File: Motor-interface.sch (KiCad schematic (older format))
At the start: 5 parts, among them K1 RELAY_2RT, U1 MCP42010, U2 Teensy_3.2

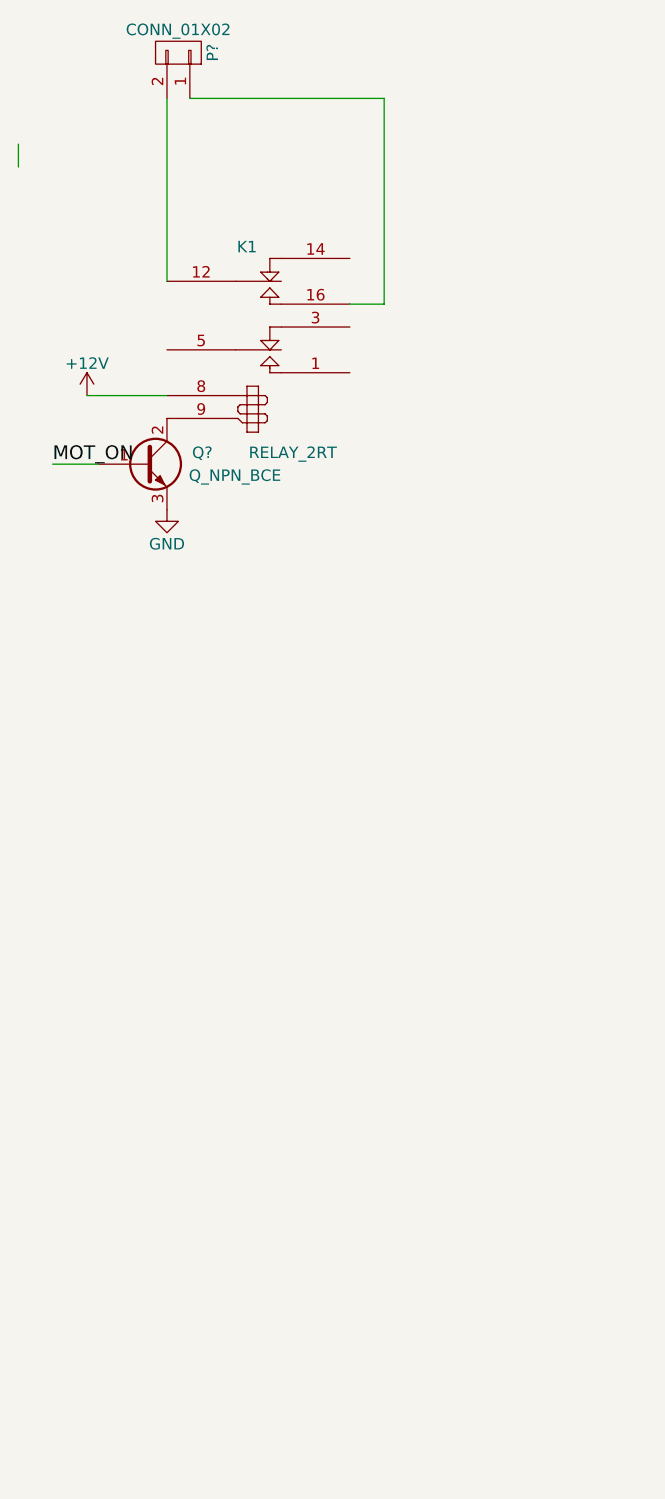
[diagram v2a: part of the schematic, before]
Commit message: Added TE 23pins and netlist
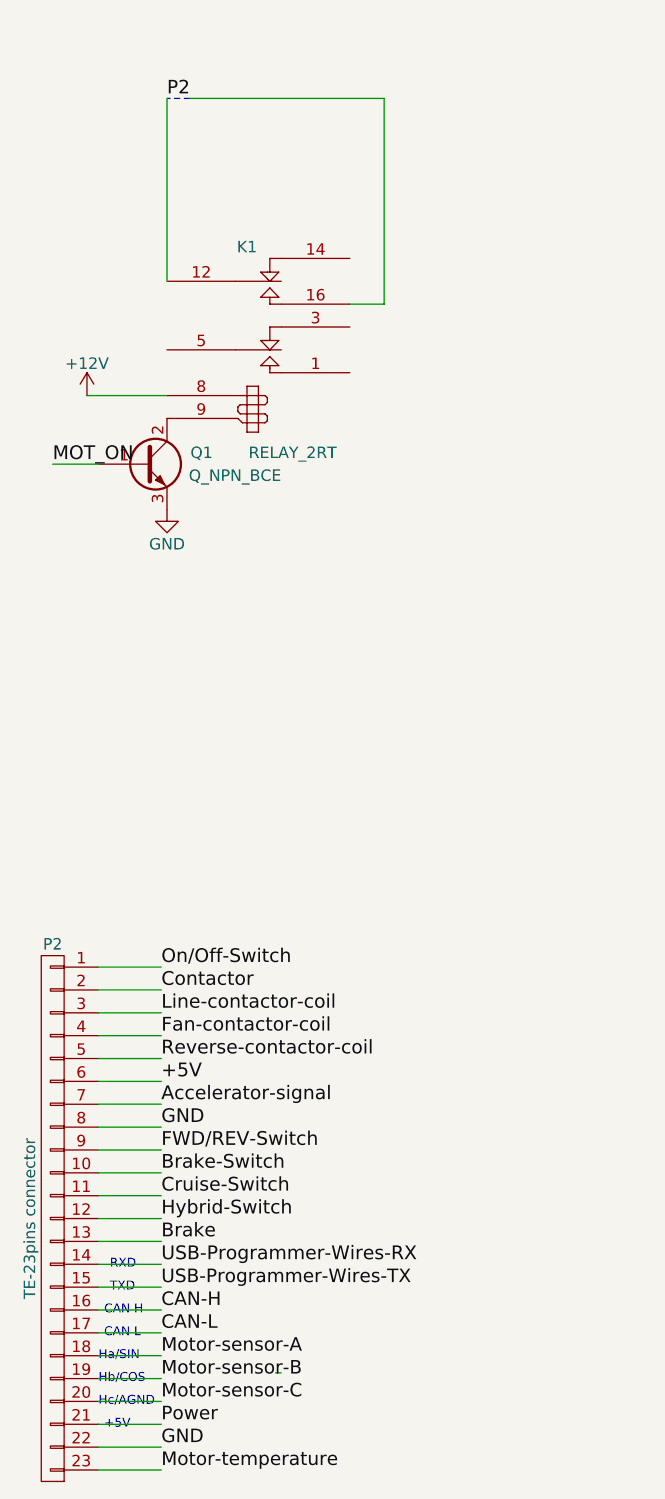
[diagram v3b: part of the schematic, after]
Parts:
- removed P?: CONN_01X02, symbol CONN_01X02
- added P2: TE-23pins connector, electric_car_lib:TE_23_pins_776087-1_connector, symbol CONN_01X23
- K1: footprint (none) -> Relays_ThroughHole:Relay_SANYOU_SRD_Series_Form_C
- Q1: renamed from Q?; footprint (none) -> TO_SOT_Packages_SMD:SOT-23
- U1: footprint (none) -> Housings_SOIC:SOIC-14_3.9x8.7mm_Pitch1.27mm
- U2: footprint (none) -> Housings_SSOP:TSSOP-32_6.1x11mm_Pitch0.65mm
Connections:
- net labels added: +5V, Accelerator-signal, Brake-Switch, CAN-H, CAN-L, Contactor, Cruise-Switch, FWD/REV-Switch, Fan-contactor-coil, Hybrid-Switch, Line-contactor-coil, Motor-sensor-A, Motor-sensor-B, Motor-sensor-C, Motor-temperature, On/Off-Switch, P2, Power, Reverse-contactor-coil, USB-Programmer-Wires-RX, USB-Programmer-Wires-TX
- wire segments 22 -> 45
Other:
- note added: "+5V"
- note added: "CAN H"
- note added: "CAN L"
- note added: "Ha/SIN"
- note added: "Hb/COS"
- note added: "Hc/AGND"
- note added: "RXD"
- note added: "TXD"
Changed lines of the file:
@@
 LIBS:contrib
 LIBS:valves
-LIBS:electric_car
 LIBS:Motor-interface-cache
 EELAYER 25 0
@@
 F 0 "U2" H 7050 2700 39  0000 C CNN
 F 1 "Teensy_3.2" H 7050 3400 39  0000 C CNN
-F 2 "" H 6750 2400 39  0000 C CNN
+F 2 "Housings_SSOP:TSSOP-32_6.1x11mm_Pitch0.65mm" H 6750 2400 39  0001 C CNN
 F 3 "" H 6750 2400 39  0000 C CNN
 	1    7050 2850
@@
 F 0 "U1" H 4850 2900 50  0000 L CNN
 F 1 "MCP42010" H 5250 2900 50  0000 L CNN
-F 2 "" H 5150 2550 50  0000 C CNN
+F 2 "Housings_SOIC:SOIC-14_3.9x8.7mm_Pitch1.27mm" H 5150 2550 50  0001 C CNN
 F 3 "" H 5150 2550 50  0000 C CNN
 	1    5150 2450
@@
 F 0 "K1" H 1850 2600 50  0000 C CNN
 F 1 "RELAY_2RT" H 2050 1700 50  0000 C CNN
-F 2 "" H 1900 2200 50  0000 C CNN
+F 2 "Relays_ThroughHole:Relay_SANYOU_SRD_Series_Form_C" H 1900 2200 50  0001 C CNN
 F 3 "" H 1900 2200 50  0000 C CNN
 	1    1900 2200
@@
 $EndComp
 $Comp
-L Q_NPN_BCE Q?
+L Q_NPN_BCE Q1
 U 1 1 57FCBE60
 P 1400 2750
-F 0 "Q?" H 1700 2800 50  0000 R CNN
+F 0 "Q1" H 1700 2800 50  0000 R CNN
 F 1 "Q_NPN_BCE" H 2000 2700 50  0000 R CNN
-F 2 "" H 1600 2850 50  0000 C CNN
+F 2 "TO_SOT_Packages_SMD:SOT-23" H 1600 2850 50  0001 C CNN
 F 3 "" H 1400 2750 50  0000 C CNN
 	1    1400 2750
@@
 	1150 2450 1500 2450
 $Comp
-L +12V #PWR?
+L +12V #PWR01
 U 1 1 57FCC08A
 P 1150 2450
-F 0 "#PWR?" H 1150 2300 50  0001 C CNN
+F 0 "#PWR01" H 1150 2300 50  0001 C CNN
 F 1 "+12V" H 1150 2590 50  0000 C CNN
 F 2 "" H 1150 2450 50  0000 C CNN
@@
 $EndComp
 $Comp
-L GND #PWR?
+L GND #PWR02
 U 1 1 57FCC1C9
 P 1500 2950
-F 0 "#PWR?" H 1500 2700 50  0001 C CNN
+F 0 "#PWR02" H 1500 2700 50  0001 C CNN
 F 1 "GND" H 1500 2800 50  0000 C CNN
 F 2 "" H 1500 2950 50  0000 C CNN
@@
 	6000 3250 6350 3250
 $Comp
-L +3.3V #PWR?
+L +3.3V #PWR03
 U 1 1 58059323
 P 3850 2150
-F 0 "#PWR?" H 3850 2000 50  0001 C CNN
+F 0 "#PWR03" H 3850 2000 50  0001 C CNN
 F 1 "+3.3V" H 3850 2290 50  0000 C CNN
 F 2 "" H 3850 2150 50  0000 C CNN
@@
 $EndComp
 $Comp
-L +3.3V #PWR?
+L +3.3V #PWR04
 U 1 1 5805934B
 P 3850 2550
-F 0 "#PWR?" H 3850 2400 50  0001 C CNN
+F 0 "#PWR04" H 3850 2400 50  0001 C CNN
 F 1 "+3.3V" H 3850 2690 50  0000 C CNN
 F 2 "" H 3850 2550 50  0000 C CNN
@@
 Wire Wire Line
 	3850 2550 4650 2550
-$Comp
-L CONN_01X02 P?
-U 1 1 5805A054
-P 1550 950
-F 0 "P?" H 1550 1100 50  0000 C CNN
-F 1 "CONN_01X02" V 1650 950 50  0000 C CNN
-F 2 "" H 1550 950 50  0000 C CNN
-F 3 "" H 1550 950 50  0000 C CNN
-	1    1550 950
-	0    1    -1   0
-$EndComp
-Wire Wire Line
-	850  1450 850  1350
 Wire Wire Line
 	1500 1150 1500 1950
@@
 	2450 2050 2300 2050
 $Comp
-L GND #PWR?
+L GND #PWR05
 U 1 1 5805B577
 P 4650 2350
-F 0 "#PWR?" H 4650 2100 50  0001 C CNN
+F 0 "#PWR05" H 4650 2100 50  0001 C CNN
 F 1 "GND" H 4650 2200 50  0000 C CNN
 F 2 "" H 4650 2350 50  0000 C CNN
@@
 $EndComp
 $Comp
-L GND #PWR?
+L GND #PWR06
 U 1 1 5805B5A1
 P 4650 2750
-F 0 "#PWR?" H 4650 2500 50  0001 C CNN
+F 0 "#PWR06" H 4650 2500 50  0001 C CNN
 F 1 "GND" H 4650 2600 50  0000 C CNN
 F 2 "" H 4650 2750 50  0000 C CNN
@@
 	1    0    0    -1
 $EndComp
+$Comp
+L CONN_01X23 P2
+U 1 1 580EFC17
+P 1000 6050
+F 0 "P2" H 1000 7250 50  0000 C CNN
+F 1 "TE-23pins connector" V 1100 6050 50  0000 C CNN
+F 2 "electric_car_lib:TE_23_pins_776087-1_connector" H 1000 6050 50  0001 C CNN
+F 3 "" H 1000 6050 50  0000 C CNN
+	1    1000 6050
+	-1   0    0    -1
+$EndComp
+Text Label 1475 4950 0    60   ~ 0
+On/Off-Switch
+Text Label 1475 5050 0    60   ~ 0
+Contactor
+Text Label 1475 5150 0    60   ~ 0
+Line-contactor-coil
+Text Label 1475 5250 0    60   ~ 0
+Fan-contactor-coil
+Text Label 1475 5350 0    60   ~ 0
+Reverse-contactor-coil
+Text Label 1475 5450 0    60   ~ 0
++5V
+Text Label 1475 5550 0    60   ~ 0
+Accelerator-signal
+Text Label 1475 5650 0    60   ~ 0
+GND
+Text Label 1475 5750 0    60   ~ 0
+FWD/REV-Switch
+Text Label 1475 5850 0    60   ~ 0
+Brake-Switch
+Text Label 1475 5950 0    60   ~ 0
+Cruise-Switch
+Text Label 1475 6050 0    60   ~ 0
+Hybrid-Switch
+Text Label 1475 6150 0    60   ~ 0
+Brake
+Text Label 1475 6250 0    60   ~ 0
+USB-Programmer-Wires-RX
+Wire Wire Line
+	1475 6350 1200 6350
+Text Notes 1250 6275 0    39   ~ 0
+RXD
+Text Notes 1250 6375 0    39   ~ 0
+TXD
+Wire Wire Line
+	1200 6250 1475 6250
+Wire Wire Line
+	1200 6450 1475 6450
+Wire Wire Line
+	1200 6550 1475 6550
+Text Notes 1225 6475 0    39   ~ 0
+CAN H
+Text Notes 1225 6575 0    39   ~ 0
+CAN L
+Text Label 1475 6450 0    59   ~ 0
+CAN-H
+Wire Wire Line
+	1200 6650 1475 6650
+Wire Wire Line
+	1200 6750 1475 6750
+Wire Wire Line
+	1200 6850 1475 6850
+Wire Wire Line
+	1200 6950 1475 6950
+Wire Wire Line
+	1200 7050 1475 7050
+Wire Wire Line
+	1200 7150 1475 7150
+Text Notes 1200 6675 0    39   ~ 0
+Ha/SIN
+Text Notes 1200 6775 0    39   ~ 0
+Hb/COS
+Text Notes 1200 6875 0    39   ~ 0
+Hc/AGND
+Text Label 1475 6750 0    59   ~ 0
+Motor-sensor-B
+Text Label 1475 6850 0    59   ~ 0
+Motor-sensor-C
+Text Label 1475 6650 0    59   ~ 0
+Motor-sensor-A
+Text Label 1475 6350 0    59   ~ 0
+USB-Programmer-Wires-TX
+Text Label 1475 6550 0    59   ~ 0
+CAN-L
+Text Notes 1225 6975 0    39   ~ 0
++5V
+Text Label 1475 6950 0    59   ~ 0
+Power
+Text Label 1475 7050 0    59   ~ 0
+GND
+Text Label 1475 7150 0    59   ~ 0
+Motor-temperature
+Wire Wire Line
+	1200 4950 1475 4950
+Wire Wire Line
+	1200 5050 1475 5050
+Wire Wire Line
+	1200 5150 1475 5150
+Wire Wire Line
+	1200 5250 1475 5250
+Wire Wire Line
+	1200 5350 1475 5350
+Wire Wire Line
+	1200 5450 1475 5450
+Wire Wire Line
+	1200 5550 1475 5550
+Wire Wire Line
+	1200 5650 1475 5650
+Wire Wire Line
+	1200 5750 1475 5750
+Wire Wire Line
+	1200 5850 1475 5850
+Wire Wire Line
+	1200 5950 1475 5950
+Wire Wire Line
+	1200 6050 1475 6050
+Wire Wire Line
+	1200 6150 1475 6150
+Wire Wire Line
+	1975 6725 2000 6725
+Text Label 1500 1150 0    59   ~ 0
+P2
+Wire Notes Line
+	1600 1150 1500 1150
 $EndSCHEMATC

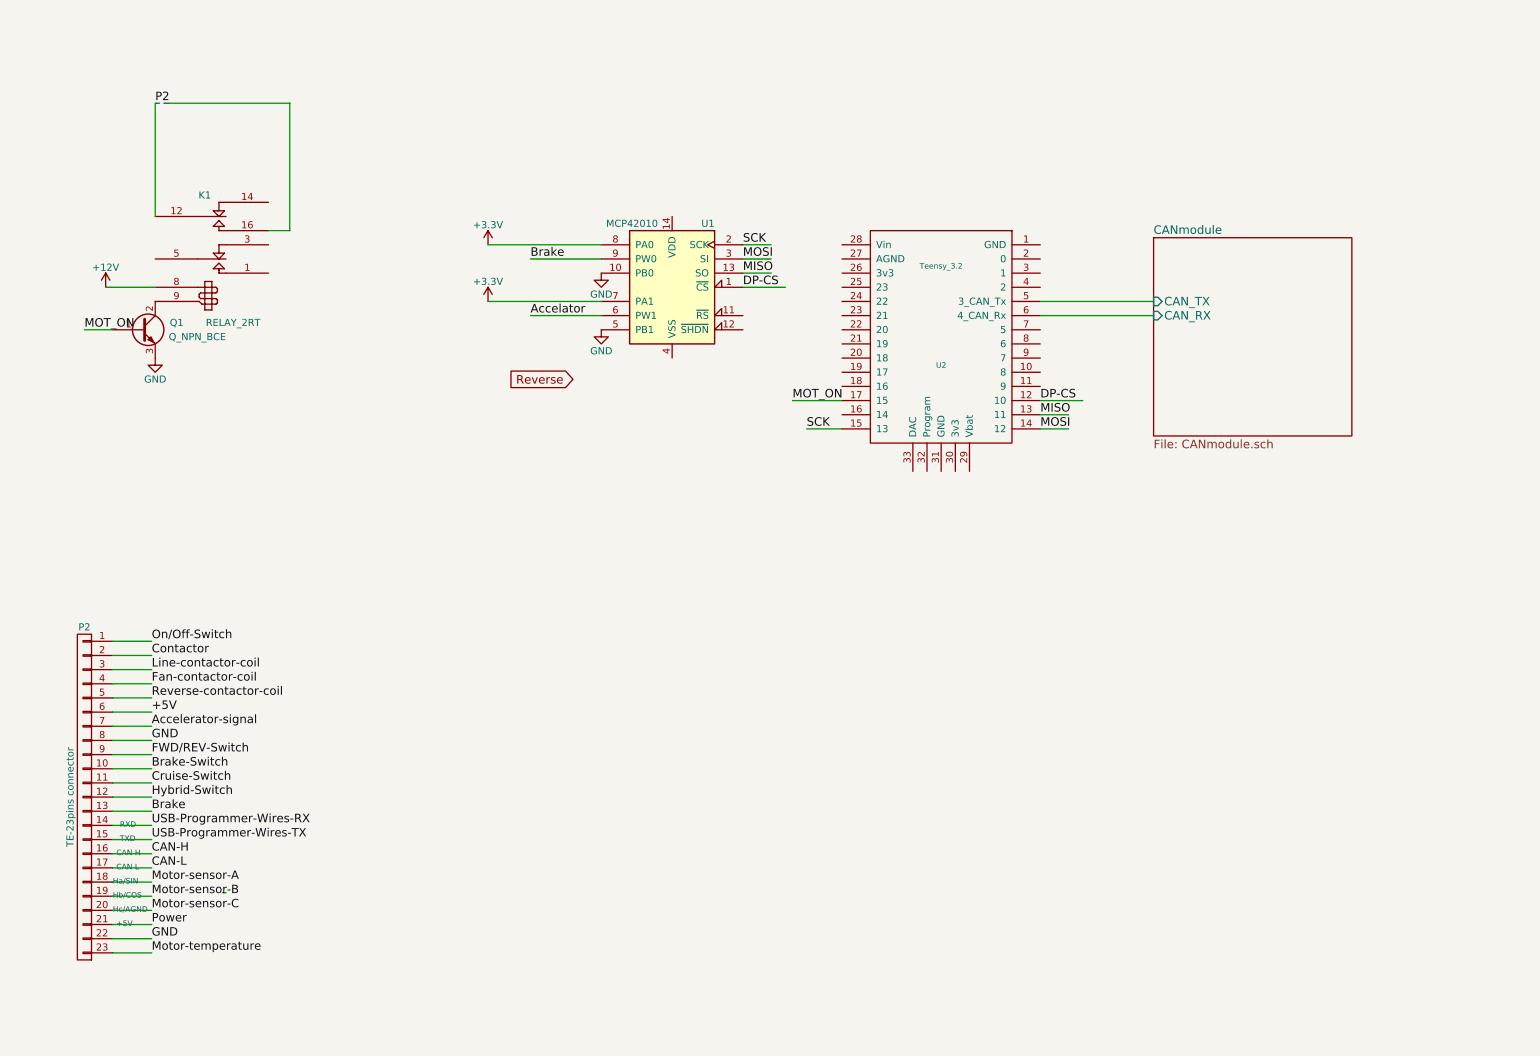
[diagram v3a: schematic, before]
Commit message: mode switches and coil contactors
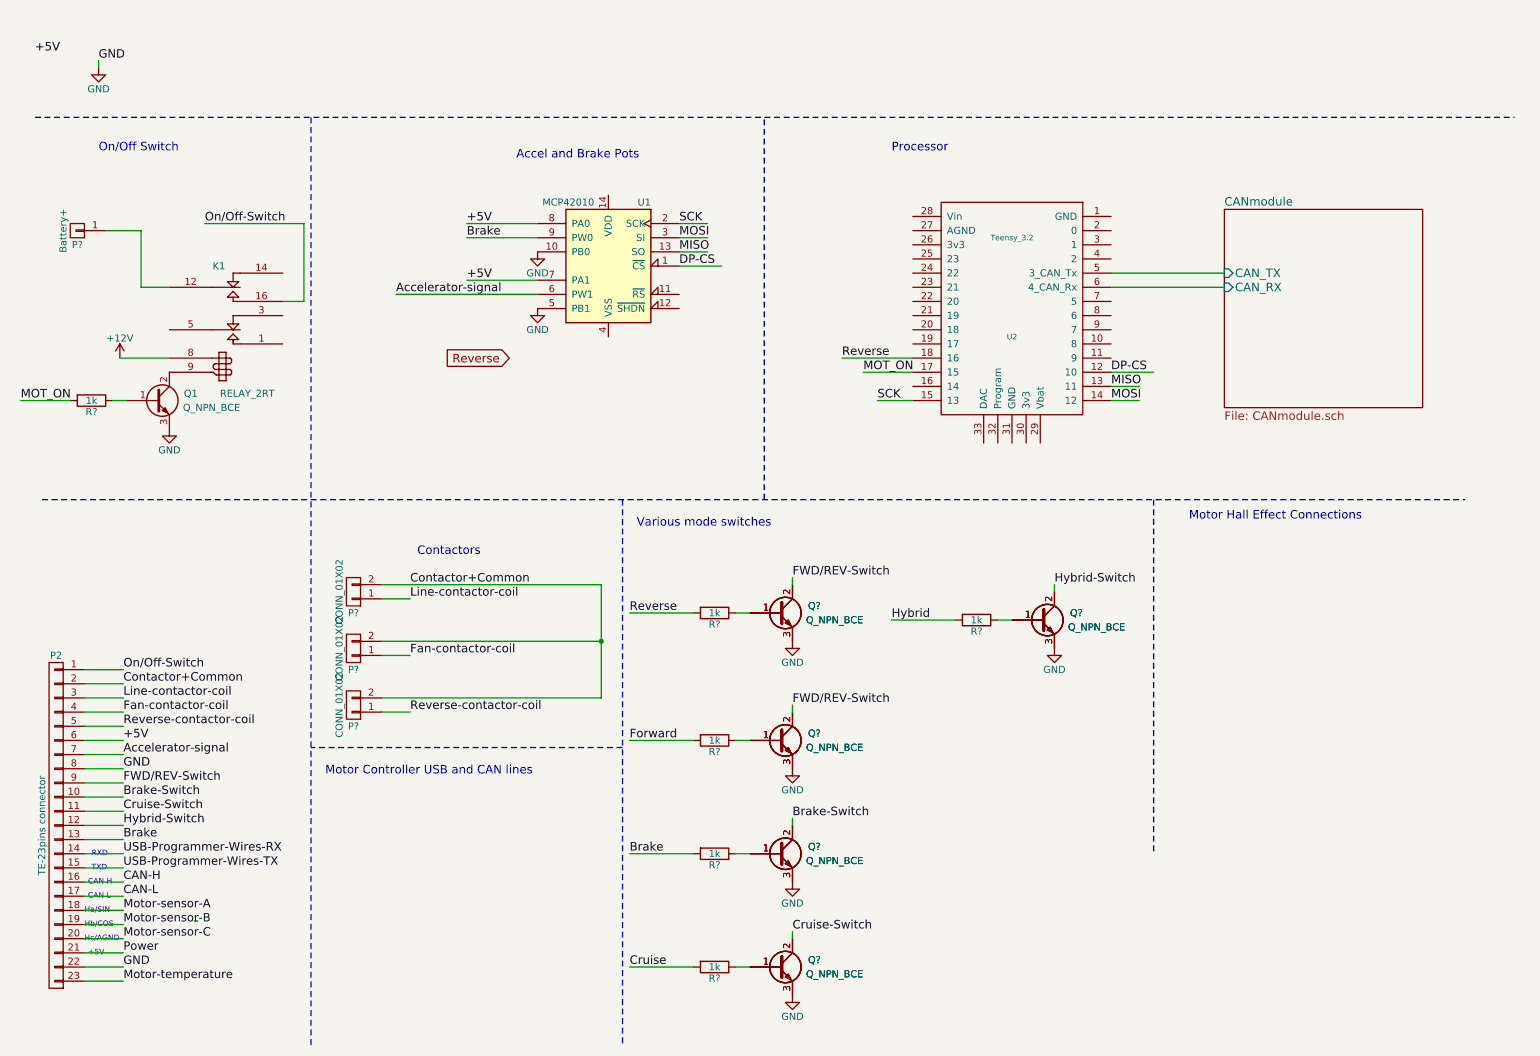
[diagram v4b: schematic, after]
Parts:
- added P?: Battery+, symbol CONN_01X01
- added P? (x3): CONN_01X02, symbol CONN_01X02
- added Q? (x10): Q_NPN_BCE, TO_SOT_Packages_SMD:SOT-23, symbol Q_NPN_BCE
- added R? (x6): 1k, symbol R
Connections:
- net labels added: Contactor+Common, Cruise, Forward, Hybrid
- net labels removed: +3.3V, Accelator, Contactor, P2
- wire segments 45 -> 72
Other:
- note added: "Accel and Brake Pots"
- note added: "Contactors"
- note added: "Motor Controller USB and CAN lines"
- note added: "Motor Hall Effect Connections"
- note added: "On/Off Switch"
- note added: "Processor"
- note added: "Various mode switches"
- moved on the sheet: K1, P2, Q1, U1, U2
